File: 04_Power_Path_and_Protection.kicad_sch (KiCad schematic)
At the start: 12 parts, among them J3 T44009_M4_POS [C481463], J4 T44009_M4_GND [C481463]

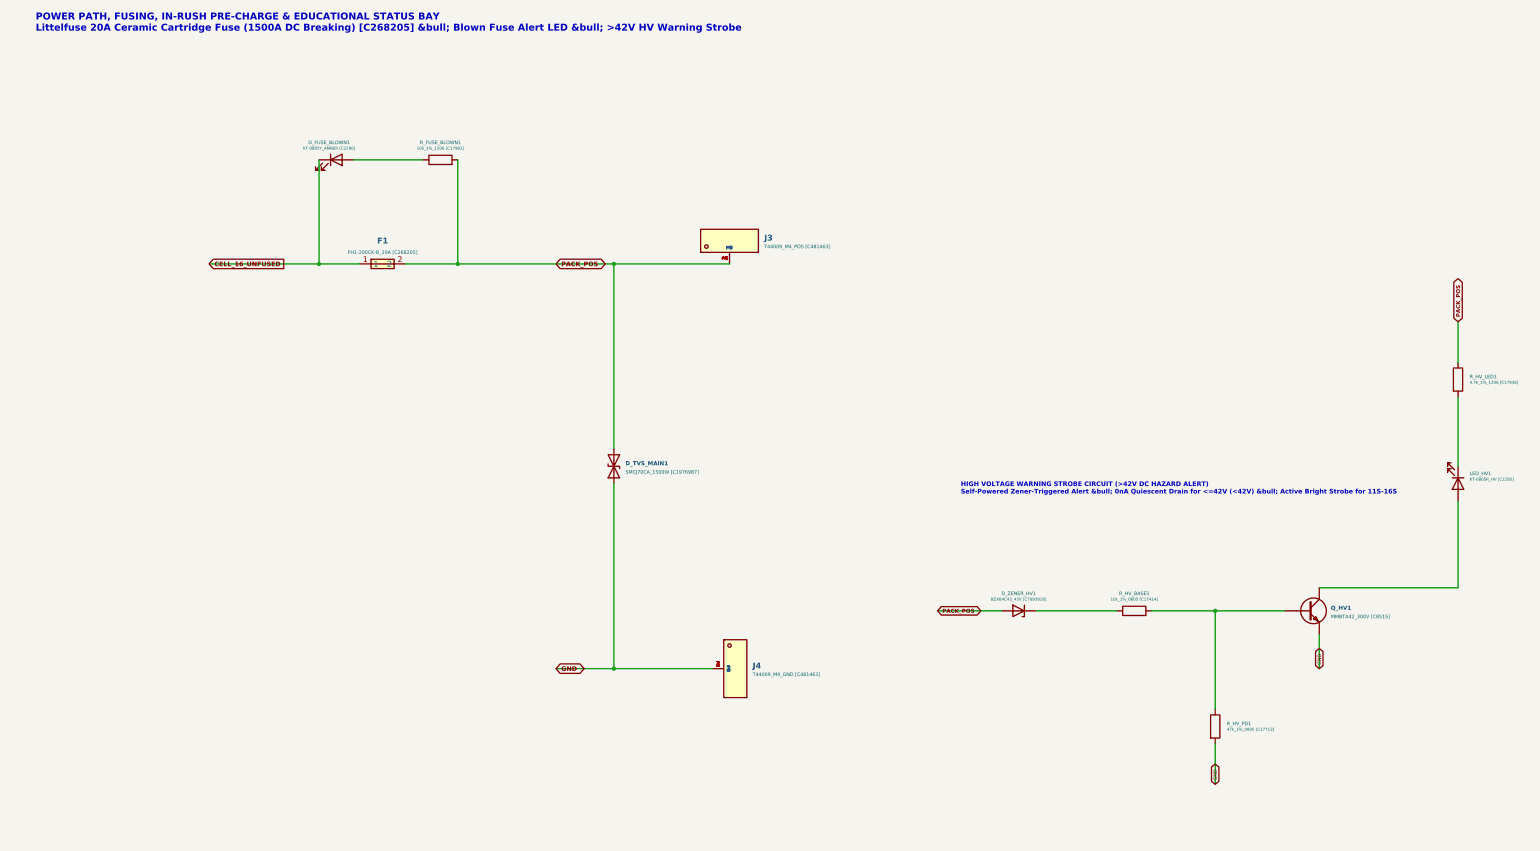
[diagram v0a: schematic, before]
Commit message: Convert pack to 14S with 7 NTC sensors, JST XH harness connectors, all-JLC BOM
- Schematic regenerated: 14 cells, 15-wire BMS sense on JST XH B15B-XH-A,
  7x 10k B3950 NTC saddles on JST XH B14B-XH-A, per-cell test loops and
  reverse-insertion indicator, power path with 5x20 fuse and M4 lugs.
- Fixes: HV zener was reversed, 4.7k/1206 HV LED resistor dissipated 0.68W
  (now 22k), 24V PPTCs on sense taps replaced with 60V MF-MSMF010-2,
  fuse-blown LED polarity corrected.
- Banana jacks (not stocked at LCSC) replaced by Keystone 5000/5001 loops.
- PCB re-laid out on the A4 (297x210) 4-layer outline: 8+6 cell columns,
  zones for cell links, sense routed on In1, NTC pairs on In2.
- ERC 0, DRC 0 (all severities), 0 unconnected, 0 schematic parity issues.
- Added Gerbers/drill zip, JLCPCB BOM + CPL, schematic PDF, renders, and the
  generator scripts in tools/.

Co-Authored-By: Claude Opus 5.5 <noreply@anthropic.com>
Claude-Session: https://claude.ai/code/session_01SDBUxKR8a94h5ECbt5NLbF
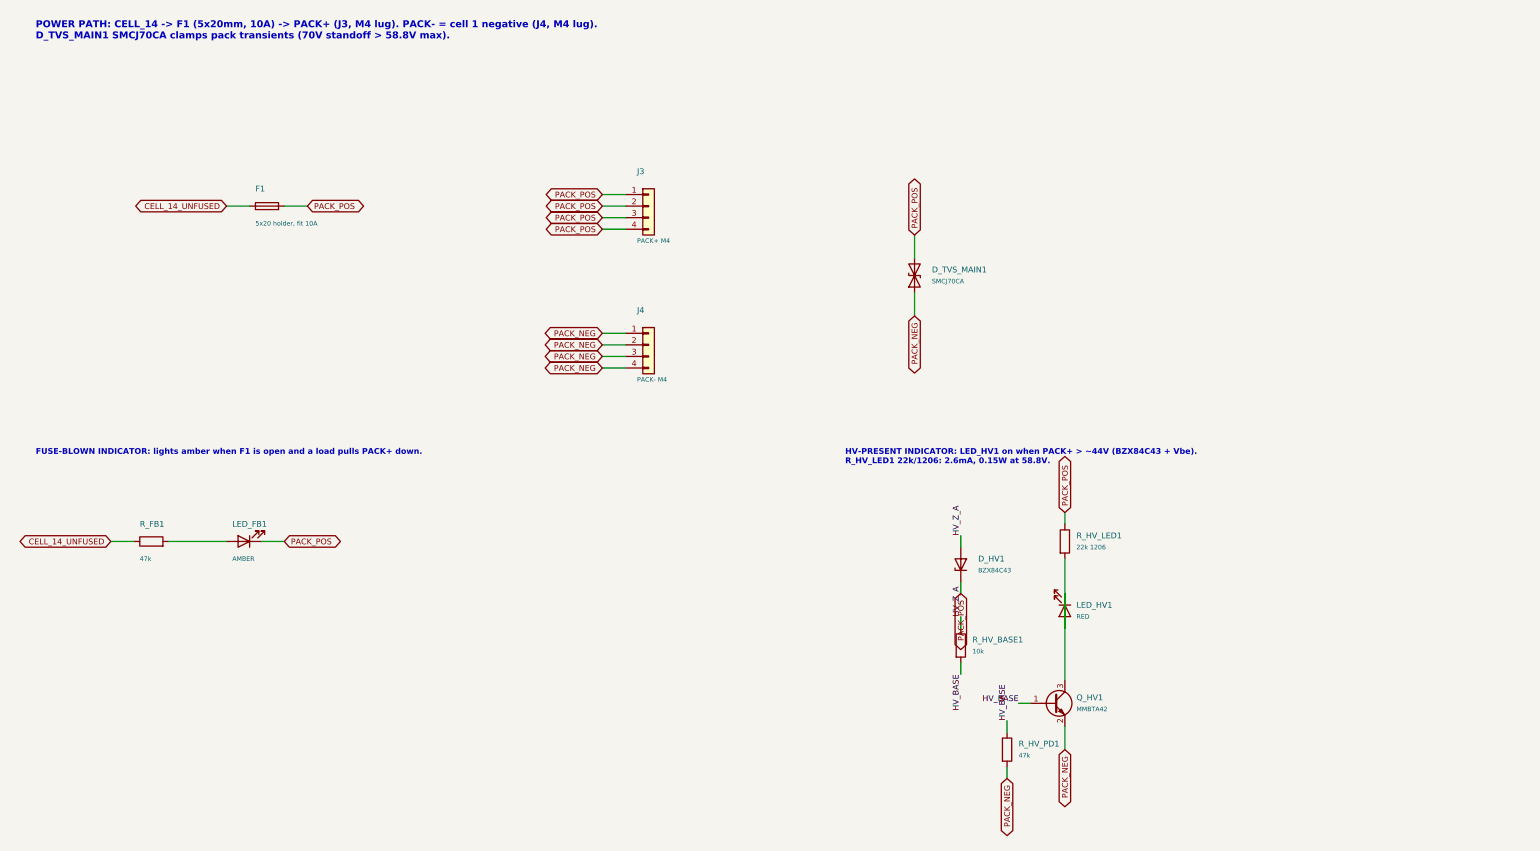
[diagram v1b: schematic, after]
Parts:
- removed D_FUSE_BLOWN1: KT-0805Y_AMBER [C2296], LED_SMD:LED_0805_2012Metric, symbol Device:LED
- removed D_ZENER_HV1: BZX84C43_43V [C7093918], Package_TO_SOT_SMD:SOT-23, symbol Device:D_Zener
- removed F1: FH1-200CK-B_20A [C268205], footprints:FUSE-TH_L24.8-W9.8-P22.60, symbol symbols:FH1-200CK-B
- removed J3: T44009_M4_POS [C481463], footprints:CONN-TH_4P-L11.1-W9.2-P5.00-T44009, symbol symbols:T44009
- removed J4: T44009_M4_GND [C481463], footprints:CONN-TH_4P-L11.1-W9.2-P5.00-T44009, symbol symbols:T44009
- removed Q_HV1: MMBTA42_300V [C8515], Package_TO_SOT_SMD:SOT-23, symbol Device:Q_NPN
- removed R_FUSE_BLOWN1: 10k_1%_1206 [C17902], Resistor_SMD:R_1206_3216Metric, symbol Device:R
- added D_HV1: BZX84C43, Package_TO_SOT_SMD:SOT-23, symbol Diode:BZX84Cxx
- added F1: 5x20 holder, fit 10A, footprints:FUSE-TH_L24.8-W9.8-P22.60, symbol Device:Fuse
- added J3: PACK+ M4, footprints:CONN-TH_4P-L11.1-W9.2-P5.00-T44009, symbol Connector_Generic:Conn_01x04
- added J4: PACK- M4, footprints:CONN-TH_4P-L11.1-W9.2-P5.00-T44009, symbol Connector_Generic:Conn_01x04
- added LED_FB1: AMBER, LED_SMD:LED_0805_2012Metric, symbol Device:LED
- added Q_HV1: MMBTA42, Package_TO_SOT_SMD:SOT-23, symbol Transistor_BJT:Q_NPN_BEC
- added R_FB1: 47k, Resistor_SMD:R_0805_2012Metric, symbol Device:R
- D_TVS_MAIN1: value SMCJ70CA_1500W [C1976987] -> SMCJ70CA; JLCPCB Part # C1976987 -> (none); LCSC C1976987 -> C840779; Manufacturer (none) -> MDD
- LED_HV1: value KT-0805R_HV [C2295] -> RED; JLCPCB Part # C2295 -> (none); LCSC C2295 -> C84256; MPN KT-0805R -> NCD0805R1; Manufacturer (none) -> NATIONSTAR
- R_HV_BASE1: value 10k_1%_0805 [C17414] -> 10k; JLCPCB Part # C17414 -> (none); Manufacturer (none) -> UNI-ROYAL
- R_HV_LED1: value 4.7k_1%_1206 [C17936] -> 22k 1206; JLCPCB Part # C17936 -> (none); LCSC C17936 -> C25830; MPN 1206W4F4701T5E -> 1206W4F2202T5E; Manufacturer (none) -> UNI-ROYAL
- R_HV_PD1: value 47k_1%_0805 [C17713] -> 47k; JLCPCB Part # C17713 -> (none); Manufacturer (none) -> UNI-ROYAL
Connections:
- net PACK_POS: now also D_HV1.3 (K), F1.2, J3.1 (Pin_1), J3.2 (Pin_2), J3.3 (Pin_3), J3.4 (Pin_4), LED_FB1.1 (K)
- net HV_BASE: now reaches R_HV_BASE1.2, R_HV_PD1.1
- net HV_BASE: now also Q_HV1.1 (B)
- net at LED_HV1.2 (A): now also LED_HV1.1 (K), R_HV_LED1.2, Q_HV1.3 (C)
- net HV_Z_A: now reaches R_HV_BASE1.1
- net HV_Z_A: now also D_HV1.1 (A)
- net GND renamed PACK_NEG
- net PACK_NEG: now also J4.1 (Pin_1), J4.2 (Pin_2), J4.3 (Pin_3), J4.4 (Pin_4), Q_HV1.2 (E)
- new net: LED_FB1.2 (A), R_FB1.2
- new net CELL_14_UNFUSED: F1.1, R_FB1.1
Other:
- note added: "FUSE-BLOWN INDICATOR: lights amber when F1 is open and a load pulls PACK+ down."
- note added: "HV-PRESENT INDICATOR: LED_HV1 on when PACK+ > ~44V (BZX84C43 + Vbe). R_HV_LED1 22k/1206: 2.6mA, 0.15W at 58.8V."
- note added: "POWER PATH: CELL_14 -> F1 (5x20mm, 10A) -> PACK+ (J3, M4 lug). PACK- = cell 1 negative (J4, M4 lug). D_TVS_MAIN1 SMCJ70CA clamps pack transients (70V standoff > 58.8V max)."
- note removed: "HIGH VOLTAGE WARNING STROBE CIRCUIT (>42V DC HAZARD ALERT) Self-Powered Zener-Triggered Alert &bull; 0nA Quiescent Drain for <=42V (<42V) &bull; Active Bright Strobe for 11S-16S"
- note removed: "POWER PATH, FUSING, IN-RUSH PRE-CHARGE & EDUCATIONAL STATUS BAY Littelfuse 20A Ceramic Cartridge Fuse (1500A DC Breaking) [C268205] &bull; Blown Fuse Alert LED &bull; >42V HV Warning Strobe"
- company: Antigravity Battery Engineering -> Battery Pack Breakout - 14S / A4
- title: POWER PATH, FUSING, HV STROBE & EDUCATIONAL STATUS BAY -> POWER PATH: FUSE, PACK TERMINALS, TVS, INDICATORS
